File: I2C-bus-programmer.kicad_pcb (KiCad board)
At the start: 2 copper layers, 85.1 x 95.2 mm, 41 parts, among them CON1 BARREL_JACK, IC1 ATMEGA328P-P, P1 FTDI_Header, P2 I2C_Header, P3 CONN_01X02, SW1 SW_Push, U1 LM7805CT, U2 PCA9543, U3 ISO1540, U4 DS1307Z+, Y1 16MHz, Y2 32.768kHz

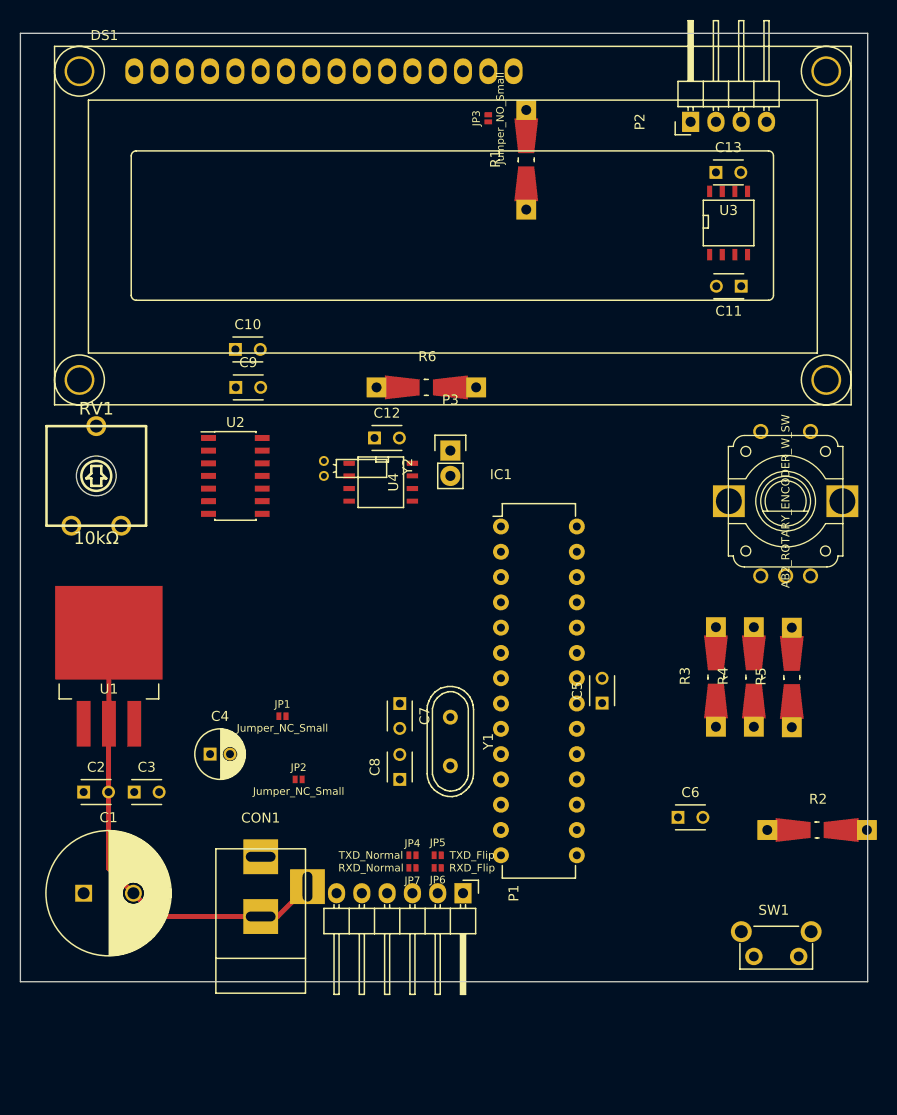
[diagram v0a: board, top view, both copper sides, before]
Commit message: Completed wiring for PCA9543 i2c bus switch. Added i2c pull-up resistors.
Wired reset pin of PCA9543 and added required pull-ups to interrupt
pins. Added pull-ups to internal i2c busses. Added switchable pull-ups
to isolated i2c bus.
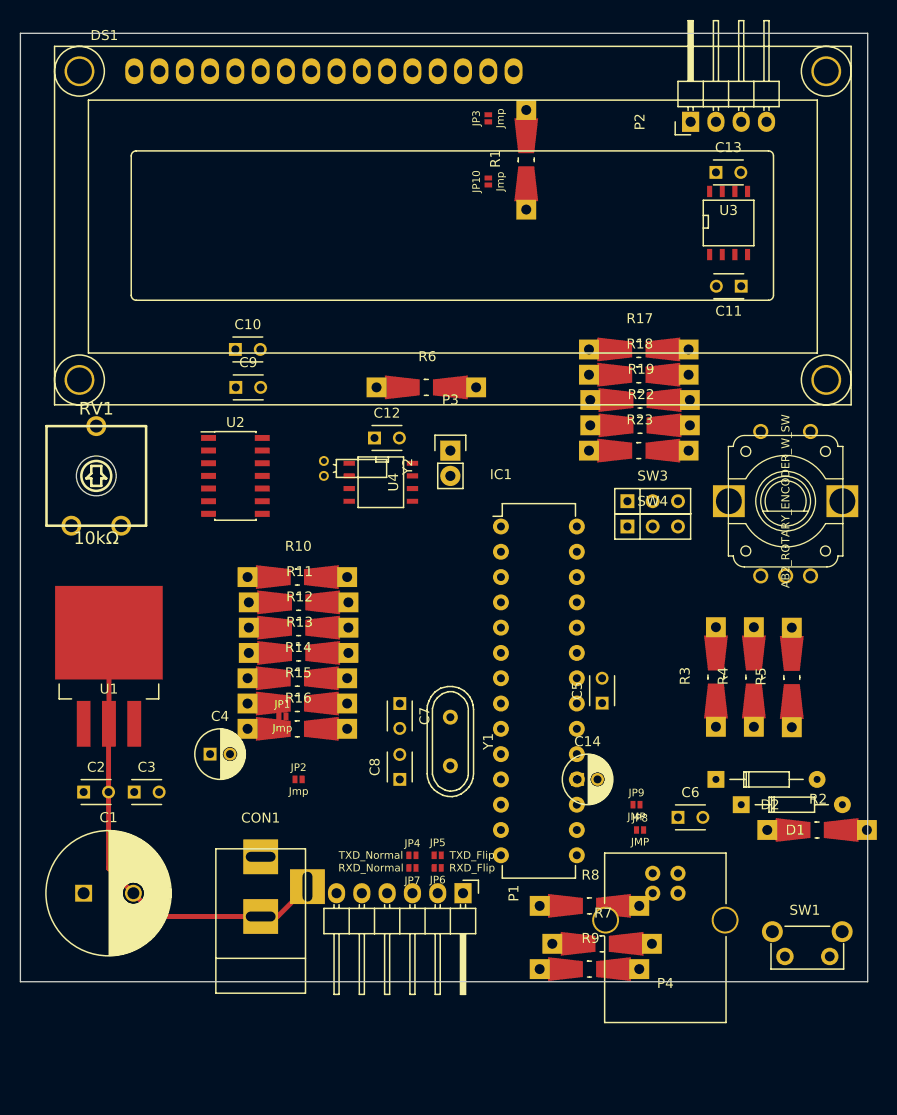
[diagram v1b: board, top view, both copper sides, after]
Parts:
- added C14: 4.7μF, Capacitors_THT:C_Radial_D5_L11_P2, F.Cu at (157.6, 109.2)
- added D1: 3.6V,0.25W, Diodes_THT:Diode_DO-35_SOD27_Horizontal_RM10, F.Cu at (174.0, 111.8)
- added D2: 3.6V,0.25W, Diodes_THT:Diode_DO-35_SOD27_Horizontal_RM10, F.Cu at (171.4, 109.2)
- added JP10: Jmp, open-project:S_JUMPER_2, F.Cu at (148.6, 49.2)
- added JP8: JMP, open-project:S_JUMPER_2, F.Cu at (163.8, 114.3)
- added JP9: JMP, open-project:S_JUMPER_2, F.Cu at (163.5, 111.8)
- added P4: USB_B, Connectors:USB_B, F.Cu at (167.6, 118.7)
- added R10: 10kΩ, Resistors_Universal:Resistor_SMD+THTuniversal_0805to1206_RM10_HandSoldering, F.Cu at (129.4, 88.9)
- added R11: 10kΩ, Resistors_Universal:Resistor_SMD+THTuniversal_0805to1206_RM10_HandSoldering, F.Cu at (129.5, 91.4)
- added R12: 10kΩ, Resistors_Universal:Resistor_SMD+THTuniversal_0805to1206_RM10_HandSoldering, F.Cu at (129.5, 94.0)
- added R13: 10kΩ, Resistors_Universal:Resistor_SMD+THTuniversal_0805to1206_RM10_HandSoldering, F.Cu at (129.5, 96.5)
- added R14: 4.7kΩ, Resistors_Universal:Resistor_SMD+THTuniversal_0805to1206_RM10_HandSoldering, F.Cu at (129.4, 99.1)
- added R15: 4.7kΩ, Resistors_Universal:Resistor_SMD+THTuniversal_0805to1206_RM10_HandSoldering, F.Cu at (129.4, 101.6)
- added R16: 4.7kΩ, Resistors_Universal:Resistor_SMD+THTuniversal_0805to1206_RM10_HandSoldering, F.Cu at (129.4, 104.1)
- added R17: 4.7kΩ, Resistors_Universal:Resistor_SMD+THTuniversal_0805to1206_RM10_HandSoldering, F.Cu at (163.7, 66.0)
- added R18: 4.7kΩ, Resistors_Universal:Resistor_SMD+THTuniversal_0805to1206_RM10_HandSoldering, F.Cu at (163.7, 68.6)
- added R19: 4.7kΩ, Resistors_Universal:Resistor_SMD+THTuniversal_0805to1206_RM10_HandSoldering, F.Cu at (163.8, 71.1)
- added R22: 4.7kΩ, Resistors_Universal:Resistor_SMD+THTuniversal_0805to1206_RM10_HandSoldering, F.Cu at (163.8, 73.7)
- added R23: 4.7kΩ, Resistors_Universal:Resistor_SMD+THTuniversal_0805to1206_RM10_HandSoldering, F.Cu at (163.7, 76.2)
- added R7: 68Ω, Resistors_Universal:Resistor_SMD+THTuniversal_0805to1206_RM10_HandSoldering, F.Cu at (160.0, 125.7)
- added R8: 68Ω, Resistors_Universal:Resistor_SMD+THTuniversal_0805to1206_RM10_HandSoldering, F.Cu at (158.8, 121.9)
- added R9: 2.2kΩ, Resistors_Universal:Resistor_SMD+THTuniversal_0805to1206_RM10_HandSoldering, F.Cu at (158.8, 128.3)
- added SW3: SW_SPDT, Buttons_Switches_THT:SW_Micro_SPST, F.Cu at (165.1, 81.3)
- added SW4: SW_SPDT, Buttons_Switches_THT:SW_Micro_SPST, F.Cu at (165.1, 83.8)
- JP1, JP2: value Jumper_NC_Small -> Jmp
- JP3: value Jumper_NO_Small -> Jmp
- moved SW1 3.12 mm to (182.9, 127.0)
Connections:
- IC1 pad 11: Lcd_D4 -> USB_Conn
- IC1 pad 13: (no net) -> i2c_reset
- IC1 pad 14: (no net) -> Lcd_D4
- IC1 pad 15: (no net) -> Lcd_D5
- IC1 pad 16: (no net) -> Lcd_D6
- IC1 pad 19: (no net) -> Lcd_D7
- IC1 pad 24: RotEnc1 -> (no net)
- IC1 pad 4: Lcd_D7 -> USB_D+
- IC1 pad 5: Lcd_D6 -> RotEnc1
- IC1 pad 6: Lcd_D5 -> USB_D-
- R1 pad 1: Net-(DS1-Pad15) -> Net-(JP10-Pad1)
- U2 pad 11: (no net) -> Net-(R13-Pad1)
- U2 pad 3: (no net) -> i2c_reset
- U2 pad 4: (no net) -> Net-(R11-Pad1)
- U2 pad 8: (no net) -> Net-(R12-Pad1)

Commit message: Added ISP header. Added protection resistors for mcu pins.
Also added flyback diode for power regulator for when powered via usb.
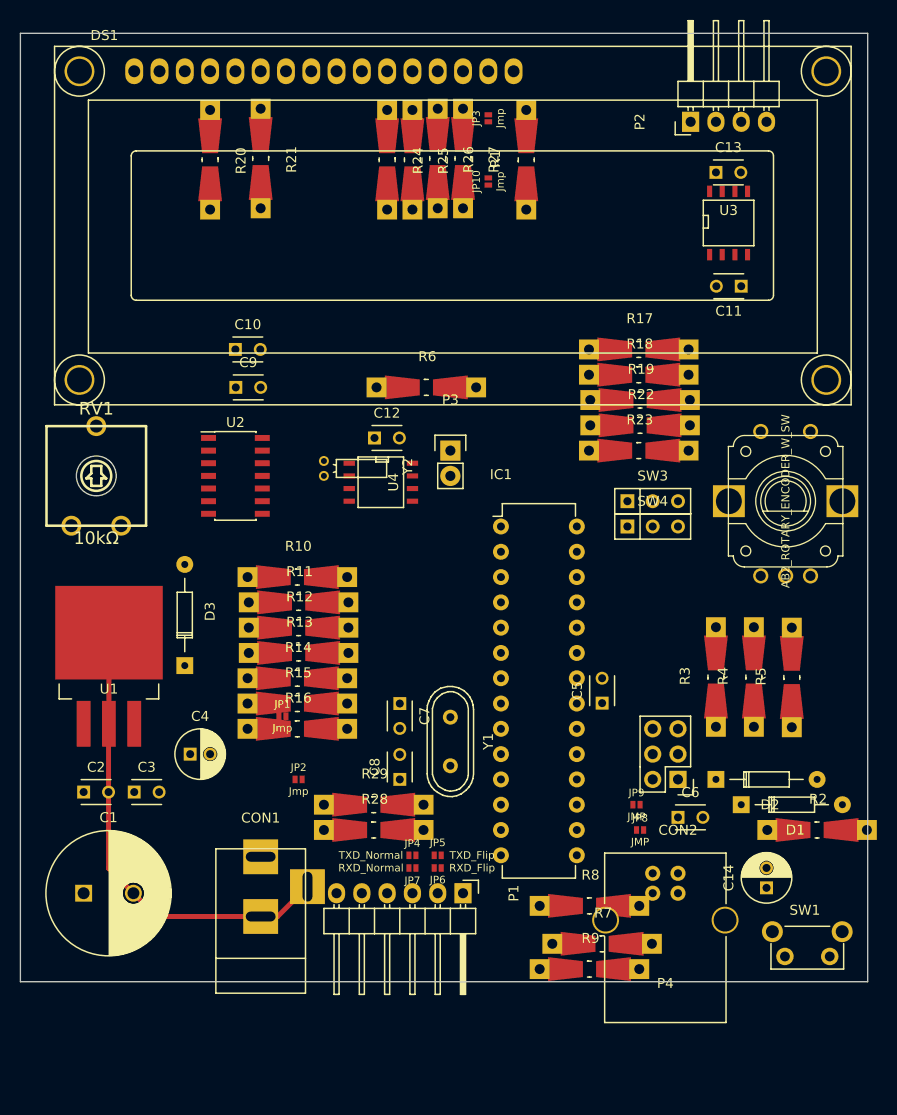
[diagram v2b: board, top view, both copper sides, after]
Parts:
- added CON2: AVR-ISP-6, Pin_Headers:Pin_Header_Straight_2x03, F.Cu at (167.6, 109.2)
- added D3: 1N4148, Diodes_THT:Diode_DO-35_SOD27_Horizontal_RM10, F.Cu at (118.1, 97.8)
- added R20: 100Ω, Resistors_Universal:Resistor_SMD+THTuniversal_0805to1206_RM10_HandSoldering, F.Cu at (120.7, 47.0)
- added R21: 100Ω, Resistors_Universal:Resistor_SMD+THTuniversal_0805to1206_RM10_HandSoldering, F.Cu at (125.7, 46.9)
- added R24: 100Ω, Resistors_Universal:Resistor_SMD+THTuniversal_0805to1206_RM10_HandSoldering, F.Cu at (138.4, 47.0)
- added R25: 100Ω, Resistors_Universal:Resistor_SMD+THTuniversal_0805to1206_RM10_HandSoldering, F.Cu at (141.0, 47.0)
- added R26: 100Ω, Resistors_Universal:Resistor_SMD+THTuniversal_0805to1206_RM10_HandSoldering, F.Cu at (143.5, 46.9)
- added R27: 100Ω, Resistors_Universal:Resistor_SMD+THTuniversal_0805to1206_RM10_HandSoldering, F.Cu at (146.1, 46.9)
- added R28: 100Ω, Resistors_Universal:Resistor_SMD+THTuniversal_0805to1206_RM10_HandSoldering, F.Cu at (137.1, 114.3)
- added R29: 100Ω, Resistors_Universal:Resistor_SMD+THTuniversal_0805to1206_RM10_HandSoldering, F.Cu at (137.1, 111.8)
- moved C14 21.9 mm to (176.5, 120.1), turned to 90 degrees
- moved C4 2.00 mm to (118.7, 106.7)
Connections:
- DS1 pad 11: Lcd_D4 -> Net-(DS1-Pad11)
- DS1 pad 12: Lcd_D5 -> Net-(DS1-Pad12)
- DS1 pad 13: Lcd_D6 -> Net-(DS1-Pad13)
- DS1 pad 14: Lcd_D7 -> Net-(DS1-Pad14)
- DS1 pad 4: Lcd_RS -> Net-(DS1-Pad4)
- DS1 pad 6: Lcd_E -> Net-(DS1-Pad6)
- IC1 pad 19: Lcd_D7 -> CLK
- JP4 pad 1: TXD -> Net-(JP4-Pad1)
- JP5 pad 1: TXD -> Net-(JP4-Pad1)
- JP6 pad 1: RXD -> Net-(JP6-Pad1)
- JP7 pad 1: RXD -> Net-(JP6-Pad1)

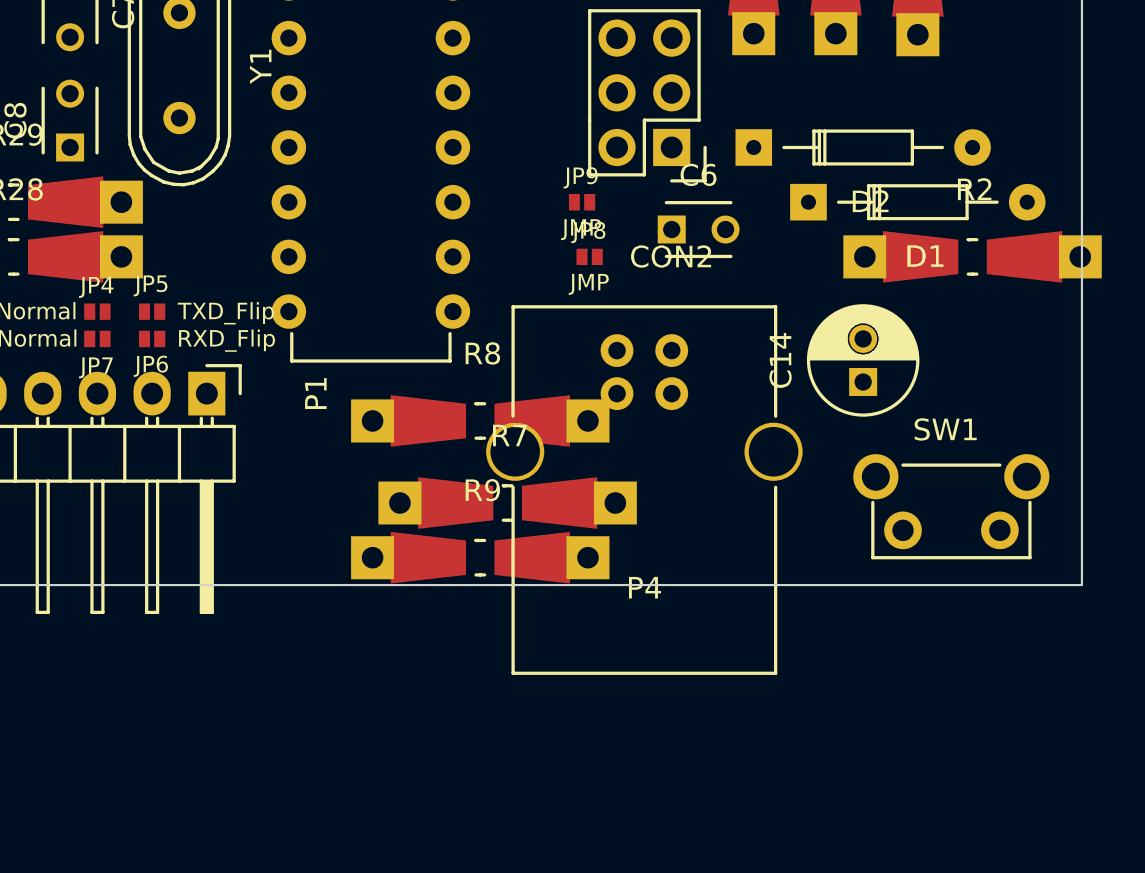
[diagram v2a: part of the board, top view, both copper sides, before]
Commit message: Reduced feature creep
Removed USB connector and circuitry.
Added proto-pads for unused MCU pins.
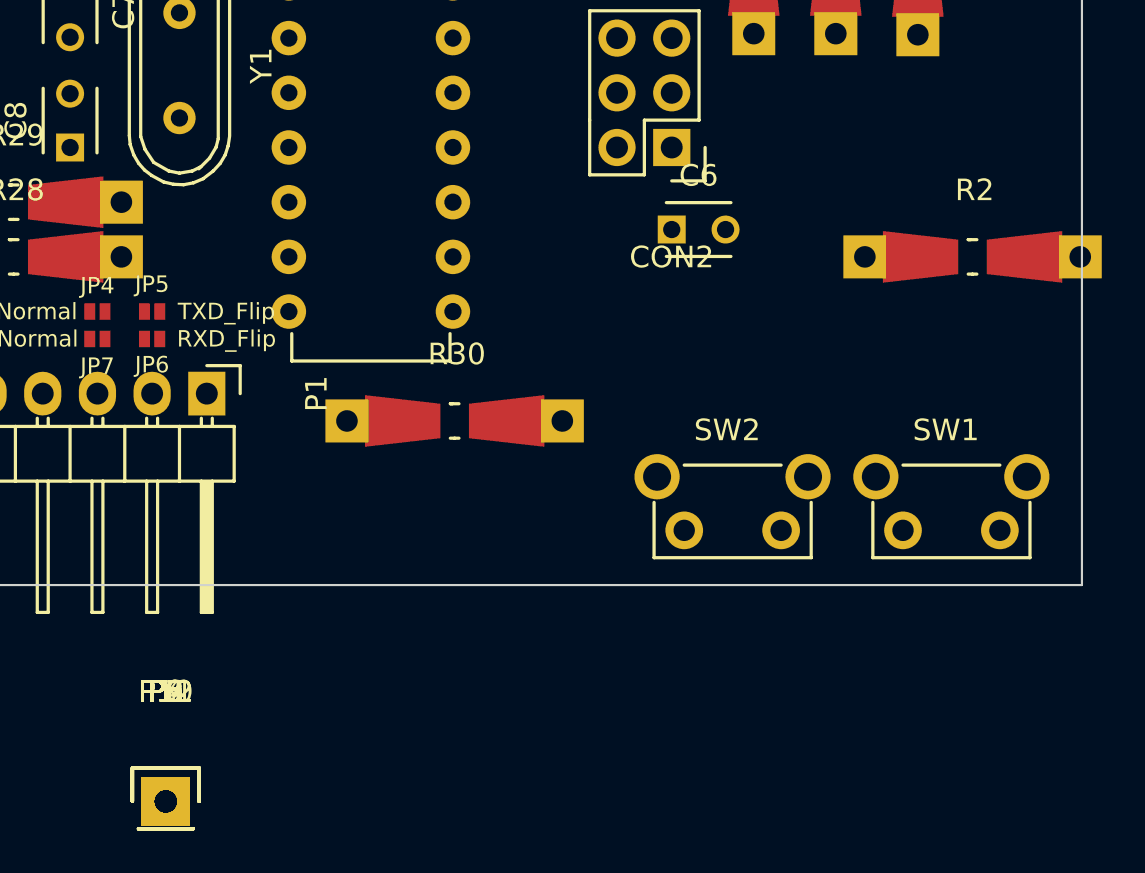
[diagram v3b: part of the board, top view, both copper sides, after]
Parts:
- removed C14: 4.7μF, Capacitors_THT:C_Radial_D5_L11_P2
- removed D1, D2: 3.6V,0.25W, Diodes_THT:Diode_DO-35_SOD27_Horizontal_RM10
- removed JP8, JP9: JMP, open-project:S_JUMPER_2
- removed R7, R8: 68Ω, Resistors_Universal:Resistor_SMD+THTuniversal_0805to1206_RM10_HandSoldering
- removed R9: 2.2kΩ, Resistors_Universal:Resistor_SMD+THTuniversal_0805to1206_RM10_HandSoldering
- added P10, P11, P12, P5, P6, P7, P8, P9: CONN_01X01, Pin_Headers:Pin_Header_Straight_1x01, F.Cu at (144.1, 139.6)
- added R30: 10kΩ, Resistors_Universal:Resistor_SMD+THTuniversal_0805to1206_RM10_HandSoldering, F.Cu at (157.6, 121.9)
- added SW2: SW_Push, Buttons_Switches_THT:SW_Tactile_SPST_Angled, F.Cu at (172.7, 127.0)
- P4: value USB_B -> CONN_01X01; footprint Connectors:USB_B -> Pin_Headers:Pin_Header_Straight_1x01
- moved P4 31.5 mm to (144.1, 139.6), turned to 0 degrees
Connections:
- DS1 pad 10: (no net) -> Net-(DS1-Pad10)
- DS1 pad 7: (no net) -> Net-(DS1-Pad7)
- DS1 pad 8: (no net) -> Net-(DS1-Pad8)
- DS1 pad 9: (no net) -> Net-(DS1-Pad9)
- IC1 pad 11: USB_Conn -> Pin_PD5
- IC1 pad 12: (no net) -> Pin_PD6
- IC1 pad 24: (no net) -> Pin_PC1
- IC1 pad 26: (no net) -> Button1
- IC1 pad 4: USB_D+ -> Pin_PD2
- IC1 pad 6: USB_D- -> Pin_PD4
- P4 pad 1: Net-(JP9-Pad1) -> Net-(P4-Pad1)
- SW3 pad 3: (no net) -> Net-(P4-Pad1)
- SW4 pad 3: (no net) -> Net-(P5-Pad1)
- U4 pad 3: (no net) -> Net-(U4-Pad3)
